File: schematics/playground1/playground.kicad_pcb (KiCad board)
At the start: 2 copper layers, 60 parts, among them J1 Conn_01x05, J2 Conn_02x03_Odd_Even, J3 Conn_01x03, J4 Conn_02x04_Odd_Even, SW1 SW_SPST, SW2 SW_Push, SW3 SW_Push, U1 ADS1299, U2 MCP1700x-330xxTT, U3 PIC32MX250F128B_I_SS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

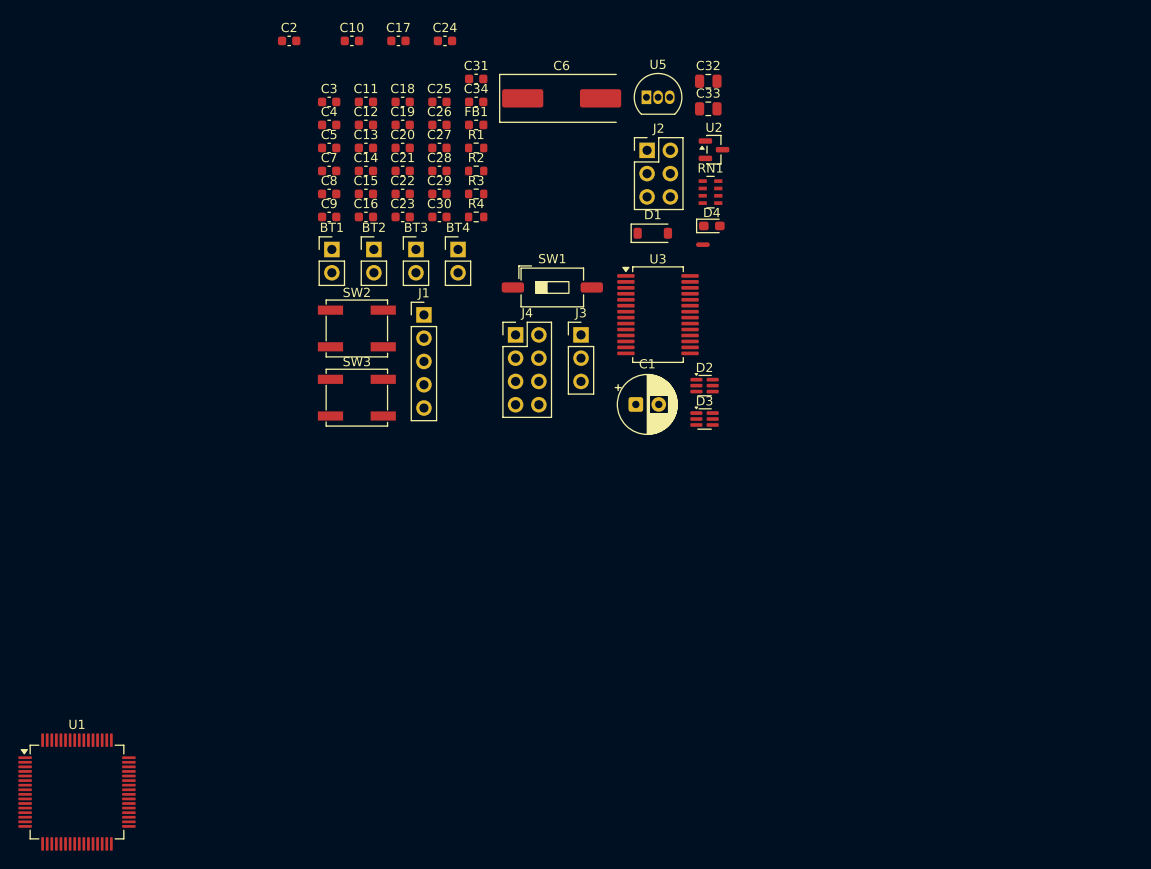
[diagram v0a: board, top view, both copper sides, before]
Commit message: organize PCB, add AGND and DGND nets, but no wiring
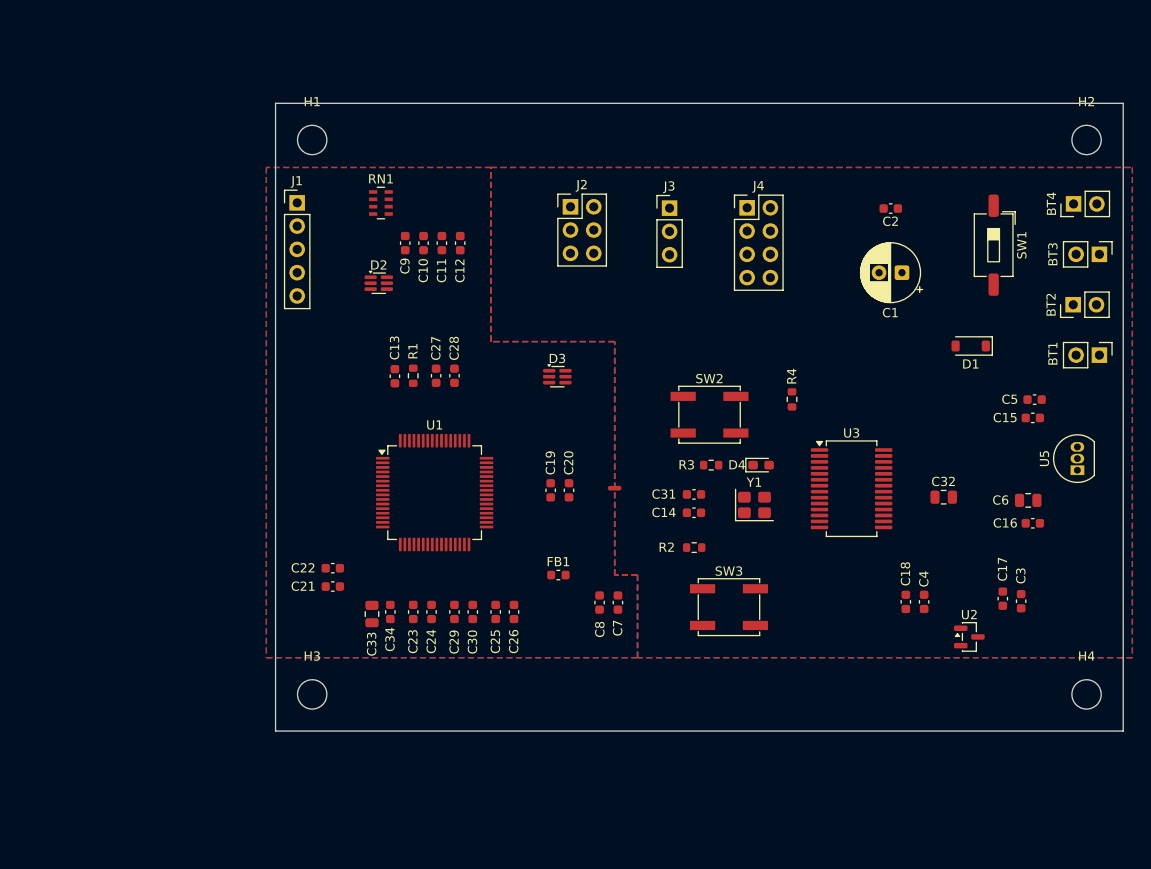
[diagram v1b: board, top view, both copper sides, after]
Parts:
- added H1: MountingHole, MountingHole:MountingHole_3.2mm_M3, F.Cu at (96.0, 70.5)
- added H2: MountingHole, MountingHole:MountingHole_3.2mm_M3, F.Cu at (180.5, 70.5)
- added H3: MountingHole, MountingHole:MountingHole_3.2mm_M3, F.Cu at (96.0, 131.0)
- added H4: MountingHole, MountingHole:MountingHole_3.2mm_M3, F.Cu at (180.5, 131.0)
- added Y1: 8MHz, Crystal:Crystal_SMD_3225-4Pin_3.2x2.5mm, F.Cu at (144.3, 110.3)
- C6: footprint Crystal:Crystal_SMD_HC49-SD -> Capacitor_SMD:C_0805_2012Metric
- moved C3 93.1 mm to (173.4, 120.8), turned to 90 degrees
- moved C17 89.7 mm to (171.4, 120.6), turned to 90 degrees
- moved BT1 84.5 mm to (181.9, 94.0), turned to -90 degrees
- moved C4 83.2 mm to (162.8, 120.9), turned to 90 degrees
- moved C5 81.7 mm to (174.8, 98.8), turned to 180 degrees
- moved C16 80.1 mm to (174.6, 112.3)
- moved C18 77.4 mm to (160.8, 120.9), turned to 90 degrees
- moved C15 76.8 mm to (174.6, 100.8), turned to 180 degrees
- moved BT2 76.6 mm to (179.0, 88.5), turned to 90 degrees
- moved BT3 74.6 mm to (181.9, 83.0), turned to -90 degrees
- moved C2 68.2 mm to (159.1, 78.0), turned to 180 degrees
- moved BT4 67.4 mm to (179.1, 77.5), turned to 90 degrees
- moved C6 67.2 mm to (174.1, 109.8)
- moved C33 66.2 mm to (102.5, 122.2), turned to -90 degrees
- moved C24 62.3 mm to (109.0, 122.0), turned to -90 degrees
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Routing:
- added copper zone on B.Cu, net /AGND
- added copper zone on F.Cu, net /AGND
- added copper zone on B.Cu, net /DGND
- added copper zone on F.Cu, net /DGND
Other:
- board outline added: 92.5 x 68.5 mm

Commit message: wiring and generating gerber files
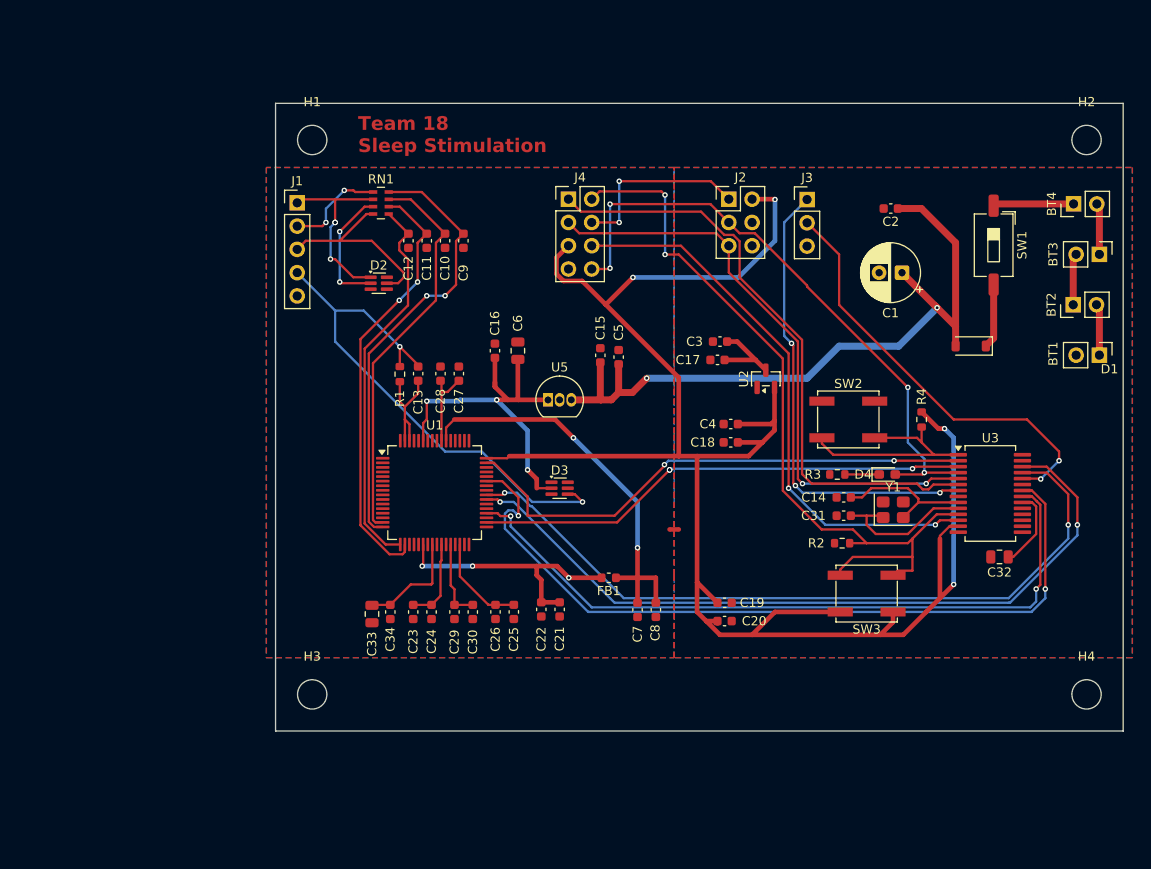
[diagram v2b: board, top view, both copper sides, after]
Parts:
- moved C16 61.6 mm to (115.9, 93.5), turned to 90 degrees
- moved U5 58.3 mm to (121.7, 98.9), turned to 0 degrees
- moved C6 58.0 mm to (118.4, 93.5), turned to -90 degrees
- moved C15 47.7 mm to (127.4, 94.0), turned to 90 degrees
- moved C5 45.6 mm to (129.4, 94.2), turned to 90 degrees
- moved C3 43.4 mm to (140.5, 92.5), turned to 180 degrees
- moved C17 40.6 mm to (140.2, 94.5), turned to 180 degrees
- moved U2 35.9 mm to (145.5, 96.6), turned to 90 degrees
- moved C4 28.7 mm to (141.7, 101.5), turned to 180 degrees
- moved C18 25.8 mm to (141.7, 103.5), turned to 180 degrees
- moved C21 24.9 mm to (123.0, 121.7), turned to 90 degrees
- moved C22 23.2 mm to (121.0, 121.7), turned to -90 degrees
- moved C19 22.6 mm to (141.0, 121.0), turned to 180 degrees
- moved C20 22.2 mm to (141.0, 123.0), turned to 0 degrees
- moved J4 19.5 mm to (124.0, 77.0)
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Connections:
- C13 pad 1: /BIAS_DRV -> /BIAS
- C14 pad 1: /AGND -> /DGND
- C31 pad 2: /AGND -> /DGND
- C32 pad 2: /AGND -> /DGND
- R1 pad 1: /BIAS_DRV -> /BIAS
- R2 pad 2: /AGND -> /DGND
- R3 pad 1: /AGND -> /DGND
- SW2 pad 1: /AGND -> /DGND
- U3 pad 19: /AGND -> /DGND
- U3 pad 27: /AGND -> /DGND
- U3 pad 8: /AGND -> /DGND
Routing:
- net /DVDD_3V3: track 0.00 -> 199.4 mm, vias 0 -> 4
- net /MISO: track 0.00 -> 86.8 mm, vias 0 -> 2
- net /BOOT_EN: track 0.00 -> 86.6 mm, vias 0 -> 2
- net /CS1: track 0.00 -> 83.7 mm, vias 0 -> 2
- net /SCLK: track 0.00 -> 81.9 mm, vias 0 -> 2
- net /VBAT_PROT: track 0.00 -> 79.0 mm, vias 0 -> 2
- net /AVDD_5V: track 0.00 -> 78.5 mm, vias 0 -> 6
- net /RESET: track 0.00 -> 78.2 mm, vias 0 -> 2
- net /PGD: track 0.00 -> 66.9 mm, vias 0 -> 4
- net /D13: track 0.00 -> 66.8 mm
- net /PGC: track 0.00 -> 65.1 mm, vias 0 -> 2
- net /D18: track 0.00 -> 61.5 mm, vias 0 -> 2
- net /BIAS: track 0.00 -> 59.3 mm, vias 0 -> 2
- net /DRDY: track 0.00 -> 57.7 mm, vias 0 -> 2
- net /MOSI: track 0.00 -> 54.2 mm, vias 0 -> 3
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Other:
- board text added: "Team 18 Sleep Stimulation"

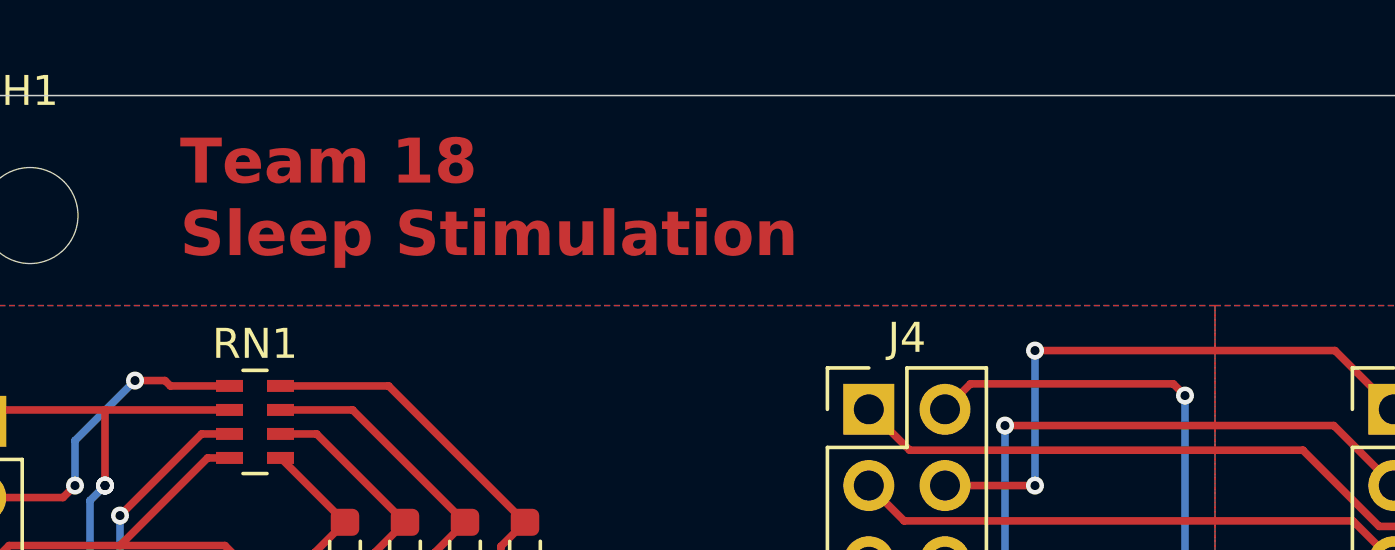
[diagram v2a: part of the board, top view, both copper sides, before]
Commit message: change power subsystem to be dgnd, generate gerbers
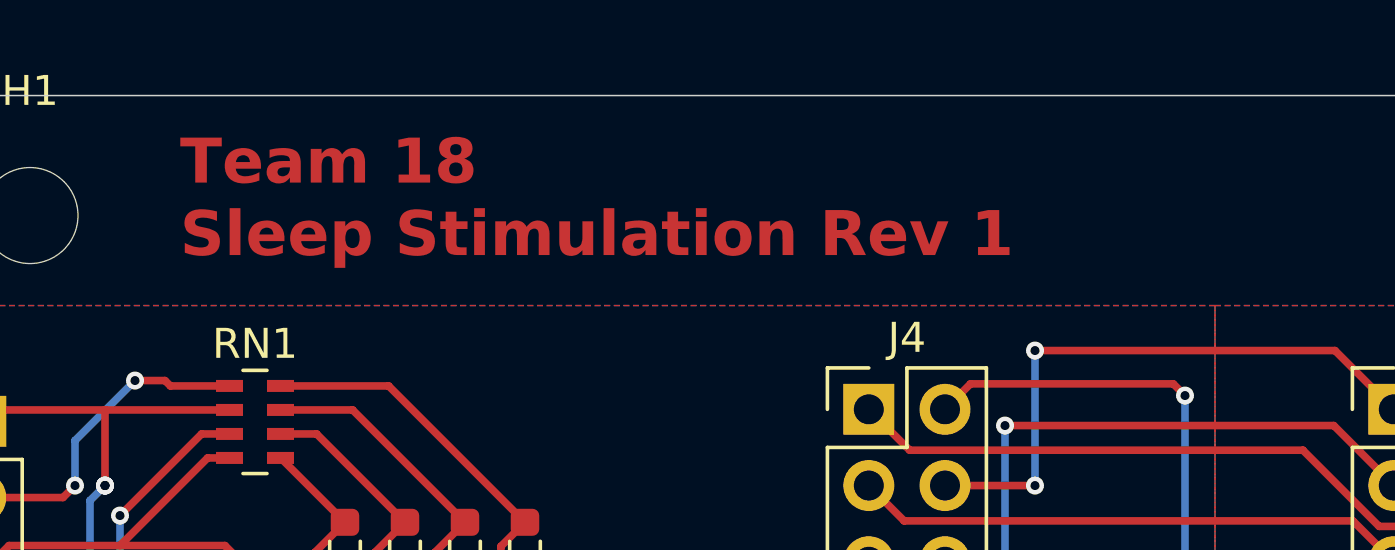
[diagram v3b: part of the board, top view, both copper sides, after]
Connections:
- BT1 pad 2: /AGND -> /DGND
- C1 pad 2: /AGND -> /DGND
- C2 pad 2: /AGND -> /DGND
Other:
- board text added: "Team 18 Sleep Stimulation Rev 1"
- board text removed: "Team 18 Sleep Stimulation"
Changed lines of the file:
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@@
 			(layers "*.Cu" "*.Mask")
 			(remove_unused_layers no)
-			(net 2 "/AGND")
+			(net 7 "/DGND")
 			(pintype "passive")
 		)
@@
 			(layers "F.Cu" "F.Mask" "F.Paste")
 			(roundrect_rratio 0.25)
-			(net 2 "/AGND")
+			(net 7 "/DGND")
 			(pintype "passive")
 		)
@@
 			(layers "*.Cu" "*.Mask")
 			(remove_unused_layers no)
-			(net 2 "/AGND")
+			(net 7 "/DGND")
 			(pinfunction "-")
 			(pintype "passive")
@@
 		(layer "Edge.Cuts")
 	)
-	(gr_text "Team 18\nSleep Stimulation"
+	(gr_text "Team 18\nSleep Stimulation Rev 1"
 		(at 101 72 0)
 		(layer "F.Cu")
@@
 		(min_thickness 0.25)
 		(filled_areas_thickness no)
-		(fill yes
+		(fill
 			(thermal_gap 0.5)
 			(thermal_bridge_width 0.5)
@@
 		(min_thickness 0.25)
 		(filled_areas_thickness no)
-		(fill yes
+		(fill
 			(thermal_gap 0.5)
 			(thermal_bridge_width 0.5)
@@
 		(min_thickness 0.25)
 		(filled_areas_thickness no)
-		(fill yes
+		(fill
 			(thermal_gap 0.5)
 			(thermal_bridge_width 0.5)
@@
 		(min_thickness 0.25)
 		(filled_areas_thickness no)
-		(fill yes
+		(fill
 			(thermal_gap 0.5)
 			(thermal_bridge_width 0.5)

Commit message: pcb sent
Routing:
- net /AVDD_5V: vias 6 -> 5
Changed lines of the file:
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@@
 		(tenting front back)
 		(pcbplotparams
-			(layerselection 0x00000000_00000000_55555555_5755f5ff)
+			(layerselection 0x00000000_00000000_55555555_575555ff)
 			(plot_on_all_layers_selection 0x00000000_00000000_00000000_00000000)
 			(disableapertmacros no)
-			(usegerberextensions no)
-			(usegerberattributes yes)
+			(usegerberextensions yes)
+			(usegerberattributes no)
 			(usegerberadvancedattributes yes)
 			(creategerberjobfile yes)
@@
 			(drillshape 0)
 			(scaleselection 1)
-			(outputdirectory "gerbers/")
+			(outputdirectory "team18__gerbers/")
 		)
 	)
@@
 			(net 2 "/AGND")
 			(pintype "passive")
+			(zone_connect 2)
 		)
 		(embedded_fonts no)
@@
 			(net 2 "/AGND")
 			(pintype "power_in")
+			(zone_connect 2)
 		)
 		(pad "4" smd roundrect
@@
 			(net 2 "/AGND")
 			(pintype "bidirectional")
+			(zone_connect 2)
 		)
 		(pad "5" smd roundrect
@@
 			(pinfunction "RESERVED")
 			(pintype "passive")
+			(zone_connect 2)
 		)
 		(embedded_fonts no)
@@
 			(pinfunction "Pin_7")
 			(pintype "passive")
+			(zone_connect 2)
 		)
 		(pad "8" thru_hole circle
@@
 			(net 2 "/AGND")
 			(pintype "passive")
+			(zone_connect 2)
 		)
 		(embedded_fonts no)
@@
 			(net 2 "/AGND")
 			(pintype "bidirectional")
+			(zone_connect 2)
 		)
 		(pad "2" smd roundrect
@@
 			(net 2 "/AGND")
 			(pintype "power_in")
+			(zone_connect 2)
 		)
 		(pad "4" smd roundrect
@@
 	(dimension
 		(type orthogonal)
-		(layer "F.Cu")
+		(layer "Dwgs.User")
 		(pts
 			(xy 96 70.5) (xy 96 131)
@@
 			(keep_text_aligned yes)
 		)
-		(gr_text "60.5"
+		(gr_text "2381.8898"
 			(at 79.7 100.75 90)
-			(layer "F.Cu")
+			(layer "Dwgs.User")
 			(effects
 				(font
@@
 	(dimension
 		(type orthogonal)
-		(layer "F.Cu")
+		(layer "Dwgs.User")
 		(pts
 			(xy 180.5 70.5) (xy 96 70.5)
@@
 			(keep_text_aligned yes)
 		)
-		(gr_text "84.5"
+		(gr_text "3326.7717"
 			(at 138.25 59.2 0)
-			(layer "F.Cu")
+			(layer "Dwgs.User")
 			(effects
 				(font
@@
 	(dimension
 		(type orthogonal)
-		(layer "F.Cu")
+		(layer "Dwgs.User")
 		(pts
 			(xy 180.5 70.5) (xy 180.5 131)
@@
 			(keep_text_aligned yes)
 		)
-		(gr_text "60.5"
+		(gr_text "2381.8898"
 			(at 189.2 100.75 90)
-			(layer "F.Cu")
+			(layer "Dwgs.User")
 			(effects
 				(font
@@
 	(dimension
 		(type orthogonal)
-		(layer "F.Cu")
+		(layer "Dwgs.User")
 		(pts
 			(xy 96 131) (xy 180.5 131)
@@
 			(keep_text_aligned yes)
 		)
-		(gr_text "84.5"
+		(gr_text "3326.7717"
 			(at 138.25 136.7 0)
-			(layer "F.Cu")
+			(layer "Dwgs.User")
 			(effects
 				(font
@@
 	)
 	(via
-		(at 124 118.275)
-		(size 0.6)
-		(drill 0.3)
-		(layers "F.Cu" "B.Cu")
-		(net 8)
-	)
-	(via
 		(at 113.5 117)
 		(size 0.6)
@@
 		(min_thickness 0.25)
 		(filled_areas_thickness no)
-		(fill
+		(fill yes
 			(thermal_gap 0.5)
 			(thermal_bridge_width 0.5)
@@
 		(min_thickness 0.25)
 		(filled_areas_thickness no)
-		(fill
+		(fill yes
 			(thermal_gap 0.5)
 			(thermal_bridge_width 0.5)
@@
 		(min_thickness 0.25)
 		(filled_areas_thickness no)
-		(fill
+		(fill yes
 			(thermal_gap 0.5)
 			(thermal_bridge_width 0.5)
@@
 		(min_thickness 0.25)
 		(filled_areas_thickness no)
-		(fill
+		(fill yes
 			(thermal_gap 0.5)
 			(thermal_bridge_width 0.5)
